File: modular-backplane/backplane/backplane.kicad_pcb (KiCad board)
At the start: 4 copper layers, 100 x 100 mm, 86 parts, among them J1 West, J10 Module, J11 Module, J12 Module, J13 Module, J14 Module, J15 Module, J16 Module, J17 Module, J18 Module, J19 Module, J2 South, J20 Module, J21 Module, J22 Module, J23 Module, J24 Module, J25 Module, J26 Module, J27 Module, J28 Module, J29 Module, J3 North, J30 Module, J31 Module, J32 Module, J33 Module, J34 Module, J35 Module, J36 Module, J37 Module, J38 Module, J39 Module, J4 East, J40 Module, J41 Module, J42 Module, J43 Module, J44 Module, J45 Module, J46 Module, J47 Module, J48 Module, J49 Module, J5 25-E900-02, J50 Module, J51 Module, J52 Module, J53 Module, J54 Module, J55 Module, J56 Module, J57 Module, J58 Module, J59 Module, J6 MGMT, J60 Module, J61 Module, J62 Module, J63 Module, J64 Module, J65 Module, J66 Module, J67 Module, J68 Module, J69 Module, J70 Module, J71 Module, J72 Module, J9 Module, SW1 A, SW2 B, SW3 C, SW4 D, SW5 E, SW6 F, SW7 G, SW8 H, U1 74HC14, U2 74HC14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

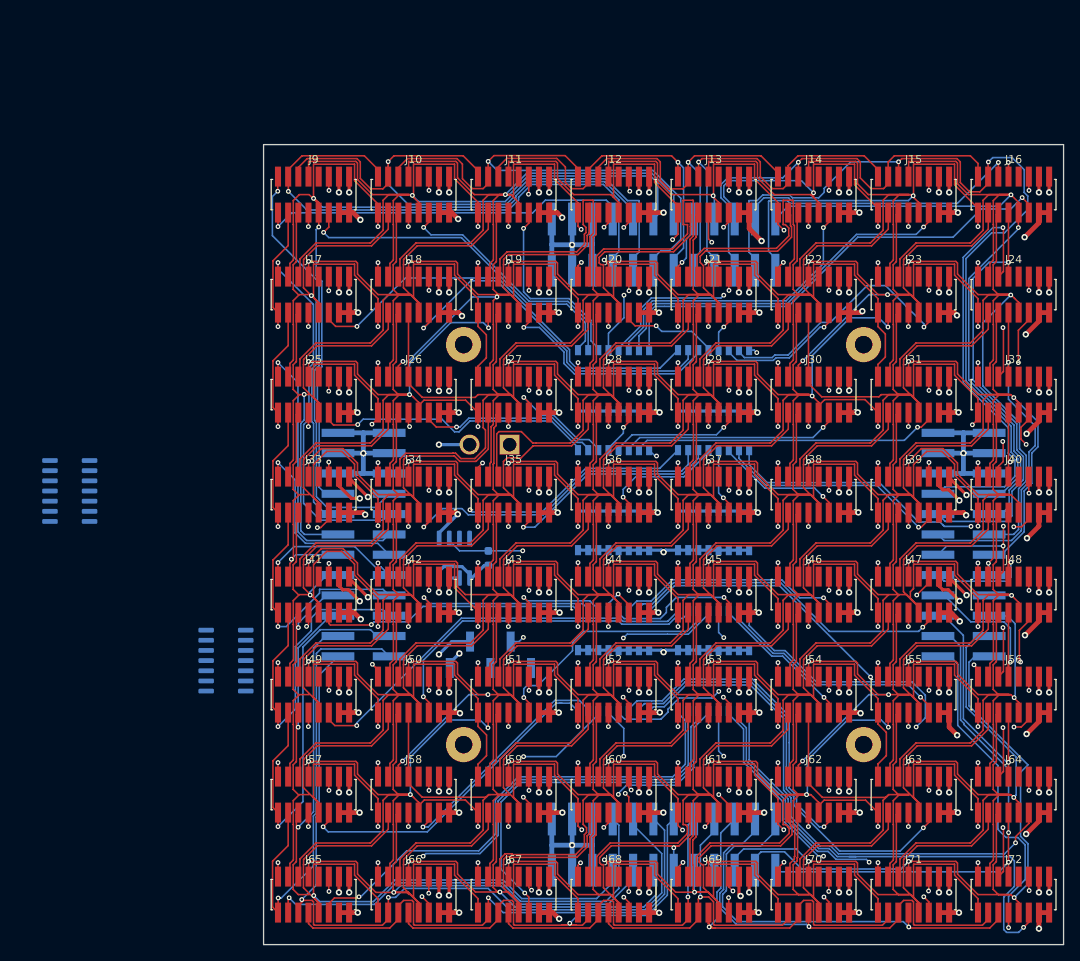
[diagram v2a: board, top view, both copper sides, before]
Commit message: Place and route clock tree; remove NRST from management header
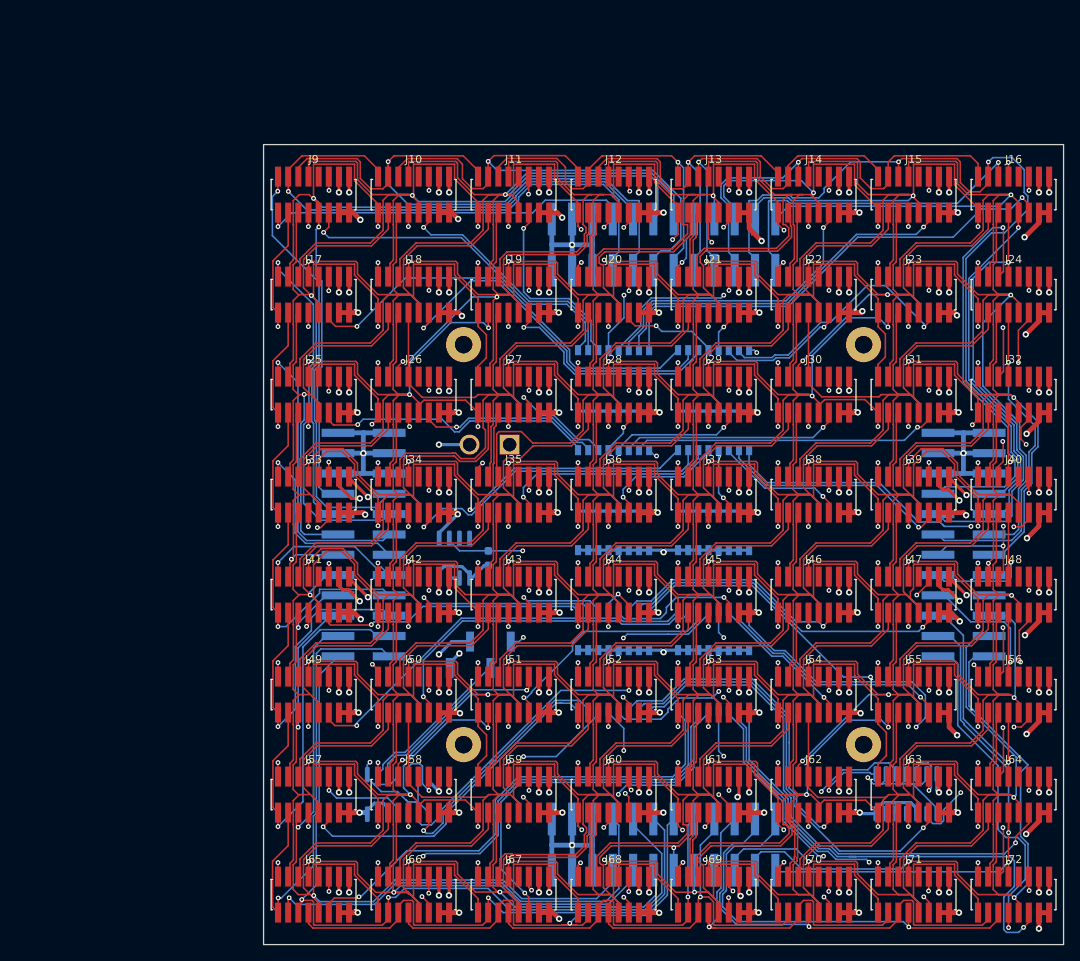
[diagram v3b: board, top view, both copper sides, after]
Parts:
- J6: footprint Connector_PinHeader_2.54mm:PinHeader_1x05_P2.54mm_Vertical_SMD_Pin1Right -> Connector_PinHeader_2.54mm:PinHeader_1x04_P2.54mm_Vertical_SMD_Pin1Right
- moved U2 111.2 mm to (130.3, 131.2), turned to 90 degrees
- moved U1 27.2 mm to (66.8, 131.2), turned to 90 degrees
- moved J6 1.27 mm to (77.1, 113.8)
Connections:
- J10 pad 9: NRST -> /Cell-A1/NRST
- J11 pad 9: NRST -> /Cell-A2/NRST
- J12 pad 9: NRST -> /Cell-A3/NRST
- J13 pad 9: NRST -> /Cell-A4/NRST
- J14 pad 9: NRST -> /Cell-A5/NRST
- J15 pad 9: NRST -> /Cell-A6/NRST
- J16 pad 9: NRST -> /Cell-A7/NRST
- J17 pad 9: NRST -> /Cell-B0/NRST
- J18 pad 9: NRST -> /Cell-B1/NRST
- J19 pad 9: NRST -> /Cell-B2/NRST
- J20 pad 9: NRST -> /Cell-B3/NRST
- J21 pad 9: NRST -> /Cell-B4/NRST
- J22 pad 9: NRST -> /Cell-B5/NRST
- J23 pad 9: NRST -> /Cell-B6/NRST
- J24 pad 9: NRST -> /Cell-B7/NRST
- J25 pad 9: NRST -> /Cell-C0/NRST
- J26 pad 9: NRST -> /Cell-C1/NRST
- J27 pad 9: NRST -> /Cell-C2/NRST
- J28 pad 9: NRST -> /Cell-C3/NRST
- J29 pad 9: NRST -> /Cell-C4/NRST
- J30 pad 9: NRST -> /Cell-C5/NRST
- J31 pad 9: NRST -> /Cell-C6/NRST
- J32 pad 9: NRST -> /Cell-C7/NRST
- J33 pad 9: NRST -> /Cell-D0/NRST
- J34 pad 9: NRST -> /Cell-D1/NRST
- J35 pad 9: NRST -> /Cell-D2/NRST
- J36 pad 9: NRST -> /Cell-D3/NRST
- J37 pad 9: NRST -> /Cell-D4/NRST
- J38 pad 9: NRST -> /Cell-D5/NRST
- J39 pad 9: NRST -> /Cell-D6/NRST
- J40 pad 9: NRST -> /Cell-D7/NRST
- J41 pad 9: NRST -> /Cell-E0/NRST
- J42 pad 9: NRST -> /Cell-E1/NRST
- J43 pad 9: NRST -> /Cell-E2/NRST
- J44 pad 9: NRST -> /Cell-E3/NRST
- J45 pad 9: NRST -> /Cell-E4/NRST
- J46 pad 9: NRST -> /Cell-E5/NRST
- J47 pad 9: NRST -> /Cell-E6/NRST
- J48 pad 9: NRST -> /Cell-E7/NRST
- J49 pad 9: NRST -> /Cell-F0/NRST
- J50 pad 9: NRST -> /Cell-F1/NRST
- J51 pad 9: NRST -> /Cell-F2/NRST
- J52 pad 9: NRST -> /Cell-F3/NRST
- J53 pad 9: NRST -> /Cell-F4/NRST
- J54 pad 9: NRST -> /Cell-F5/NRST
- J55 pad 9: NRST -> /Cell-F6/NRST
- J56 pad 9: NRST -> /Cell-F7/NRST
- J57 pad 9: NRST -> /Cell-G0/NRST
- J58 pad 9: NRST -> /Cell-G1/NRST
- J59 pad 9: NRST -> /Cell-G2/NRST
- J60 pad 9: NRST -> /Cell-G3/NRST
- J61 pad 9: NRST -> /Cell-G4/NRST
- J62 pad 9: NRST -> /Cell-G5/NRST
- J63 pad 9: NRST -> /Cell-G6/NRST
- J64 pad 9: NRST -> /Cell-G7/NRST
- J65 pad 9: NRST -> /Cell-H0/NRST
- J66 pad 9: NRST -> /Cell-H1/NRST
- J67 pad 9: NRST -> /Cell-H2/NRST
- J68 pad 9: NRST -> /Cell-H3/NRST
- J69 pad 9: NRST -> /Cell-H4/NRST
- J70 pad 9: NRST -> /Cell-H5/NRST
- J71 pad 9: NRST -> /Cell-H6/NRST
- J72 pad 9: NRST -> /Cell-H7/NRST
- J9 pad 9: NRST -> /Cell-A0/NRST
- U1 pad 1: CLK -> Net-(U1-Pad11)
- U1 pad 10: /CLK3 -> /CLK2
- U1 pad 12: (no net) -> /CLK1
- U1 pad 13: (no net) -> Net-(U1-Pad11)
- U1 pad 2: Net-(U1-Pad11) -> /CLK3
- U1 pad 5: Net-(U1-Pad11) -> GND
- U1 pad 6: /CLK1 -> unconnected-(U1-Pad6)
- U1 pad 8: /CLK2 -> Net-(U1-Pad11)
- U1 pad 9: Net-(U1-Pad11) -> CLK
- U2 pad 10: (no net) -> /CLK4
- U2 pad 11: (no net) -> Net-(U1-Pad11)
- U2 pad 12: (no net) -> /CLK6
- U2 pad 13: (no net) -> Net-(U1-Pad11)
- U2 pad 2: /CLK4 -> /CLK7
- U2 pad 3: Net-(U1-Pad11) -> GND
- U2 pad 4: /CLK5 -> unconnected-(U2-Pad4)
- U2 pad 5: Net-(U1-Pad11) -> GND
- U2 pad 6: /CLK6 -> unconnected-(U2-Pad6)
- U2 pad 8: /CLK7 -> /CLK5
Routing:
- net Net-(U1-Pad11): track 0.00 -> 101.0 mm, vias 0 -> 2
- net /CLK3: track 102.1 -> 136.8 mm
- net /CLK2: track 101.6 -> 126.5 mm
- net /CLK4: track 101.9 -> 126.0 mm, vias 8 -> 9
- net CLK: track 0.00 -> 20.0 mm
- net /CLK7: track 104.4 -> 120.6 mm, vias 8 -> 9
- net GND: track 375.8 -> 391.7 mm
- net /CLK0: track 101.8 -> 112.1 mm
- net /CLK5: track 101.6 -> 108.7 mm
- net /CLK1: track 102.1 -> 108.4 mm
- net /CLK6: track 104.0 -> 110.2 mm
- net +5V: track 1631.1 -> 1636.5 mm
- net /Cell-A4/STATE: track 83.2 -> 85.4 mm
- net /Cell-A3/STATE: track 85.8 -> 87.5 mm
- net /T-G1: track 30.0 -> 31.6 mm
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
